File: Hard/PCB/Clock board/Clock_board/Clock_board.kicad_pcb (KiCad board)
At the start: 2 copper layers, 32.1 x 21 mm, 18 parts, among them J1 Conn_01x01, J2 Conn_01x01, J3 Conn_01x01, J4 Conn_01x01, J5 Conn_01x01, J6 Conn_01x01, M1 motor, Q1 SI2302, Q2 SI2302

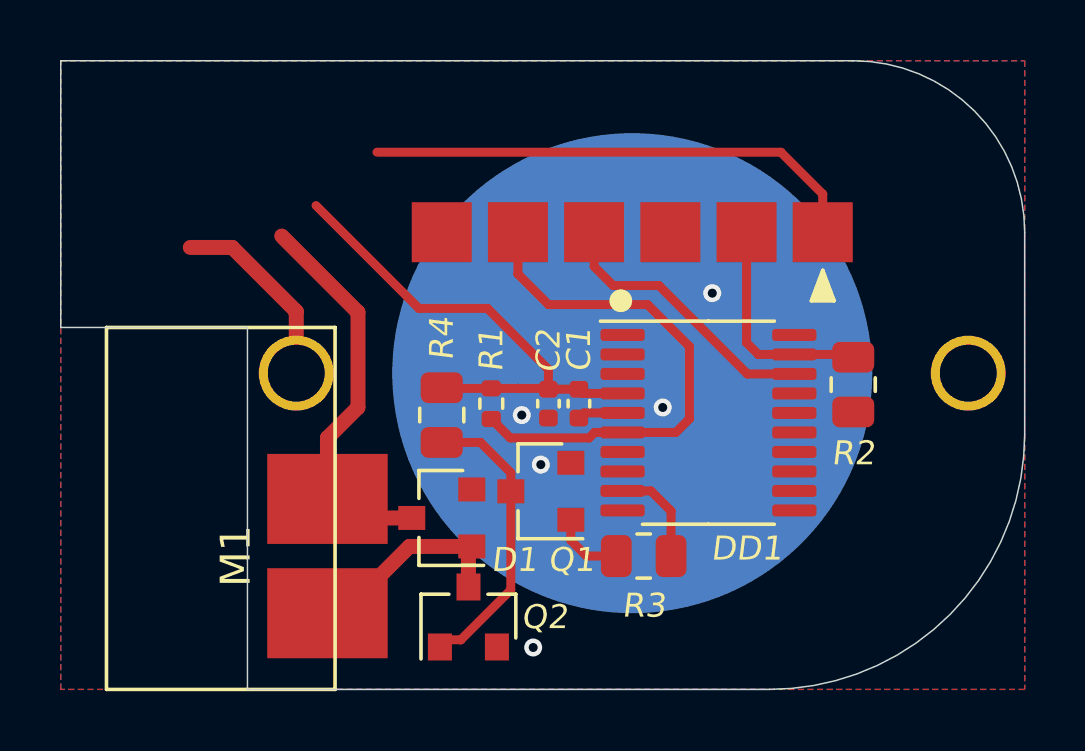
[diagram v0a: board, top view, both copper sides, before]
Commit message: shlyeha added switch component to mechanical library, changed scheme switch connection, finished pcb project
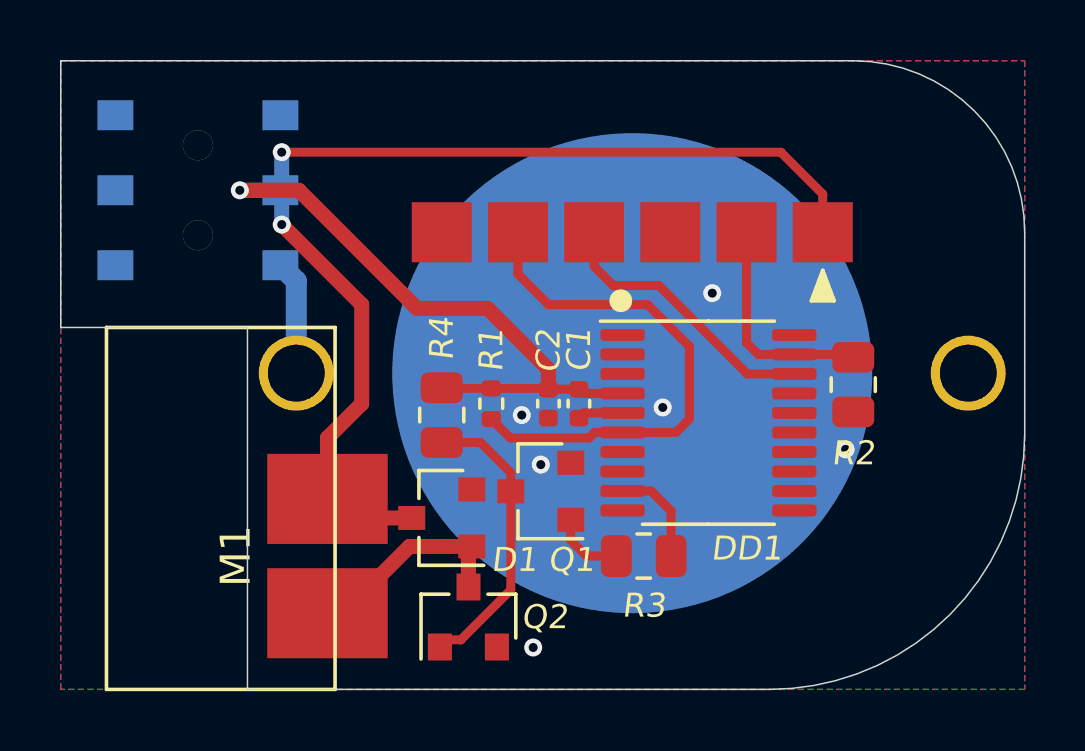
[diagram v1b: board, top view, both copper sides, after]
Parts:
- added SW1: SW_DPDT_x2, mechanical:switch_ms-22c01, B.Cu at (121.4, 74.8)
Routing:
- net +3V0: track 46.8 -> 57.0 mm, vias 0 -> 3
- net Net-(BT1-Pad1): track 6.47 -> 3.88 mm
- net GND: vias 5 -> 6
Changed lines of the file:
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@@
     (thickness 1.6)
     (drawings 13)
-    (tracks 69)
+    (tracks 80)
     (zones 0)
-    (modules 18)
-    (nets 27)
+    (modules 19)
+    (nets 28)
   )
   (page A4)
@@
   (net 25 /SWO)
   (net 26 "Net-(BT1-Pad1)")
+  (net 27 "Net-(SW1-Pad1)")
   (net_class Default "This is the default net class."
     (clearance 0.2)
@@
     (add_net "Net-(Q1-Pad1)")
     (add_net "Net-(Q1-Pad3)")
+    (add_net "Net-(SW1-Pad1)")
   )
   (module mechanical:motor_xiaomi_redmi_3s (layer F.Cu)
@@
       (scale (xyz 1 1 1))
       (rotate (xyz 0 180 0))
+    )
+  )
+  (module mechanical:switch_ms-22c01 (layer B.Cu)
+    (at 121.412 74.803 270)
+    (fp_text reference SW1 (at -3.429 -4.699) (layer B.SilkS)
+      (effects (font (size 0.8 0.8) (thickness 0.2) italic) (justify mirror))
+    )
+    (fp_text value SW_DPDT_x2 (at 0 0.5 270) (layer B.Fab) hide
+      (effects (font (size 1 1) (thickness 0.15)) (justify mirror))
+    )
+    (fp_line (start -3.81 -3.429) (end -3.81 3.429) (layer B.SilkS) (width 0.12))
+    (fp_line (start 3.81 -3.429) (end -3.81 -3.429) (layer B.SilkS) (width 0.12))
+    (fp_line (start 3.81 3.429) (end 3.81 -3.429) (layer B.SilkS) (width 0.12))
+    (fp_line (start -3.81 3.429) (end 3.81 3.429) (layer B.SilkS) (width 0.12))
+    (pad 6 smd rect (at -2.5 2.75 270) (size 1 1.2) (layers B.Cu B.Paste B.Mask))
+    (pad 5 smd rect (at 0 2.75 270) (size 1 1.2) (layers B.Cu B.Paste B.Mask))
+    (pad 4 smd rect (at 2.5 2.75 270) (size 1 1.2) (layers B.Cu B.Paste B.Mask))
+    (pad 3 smd rect (at 2.5 -2.75 270) (size 1 1.2) (layers B.Cu B.Paste B.Mask)
+      (net 26 "Net-(BT1-Pad1)"))
+    (pad 2 smd rect (at 0 -2.75 270) (size 1 1.2) (layers B.Cu B.Paste B.Mask)
+      (net 2 +3V0))
+    (pad 1 smd rect (at -2.5 -2.75 270) (size 1 1.2) (layers B.Cu B.Paste B.Mask)
+      (net 27 "Net-(SW1-Pad1)"))
+    (pad 0 thru_hole circle (at 1.5 0 270) (size 1 1) (drill 1) (layers *.Cu *.Mask))
+    (pad 0 thru_hole circle (at -1.5 0 270) (size 1 1) (drill 1) (layers *.Cu *.Mask))
+    (model C:/GitRepos/Archer/Hard/3D/STEP/g-switch_ms-22c01-g010.step
+      (at (xyz 0 0 0))
+      (scale (xyz 1 1 1))
+      (rotate (xyz 0 0 0))
     )
   )
@@
   (gr_line (start 141.859 78.486) (end 142.621 78.486) (layer F.SilkS) (width 0.12))
   (gr_line (start 142.24 77.47) (end 141.859 78.486) (layer F.SilkS) (width 0.12))
+  (via (at 143.002 83.439) (size 0.6) (drill 0.3) (layers F.Cu B.Cu) (net 1))
+  (via (at 122.809 74.803) (size 0.6) (drill 0.3) (layers F.Cu B.Cu) (net 2))
+  (via (at 124.206 73.533) (size 0.6) (drill 0.3) (layers F.Cu B.Cu) (net 2))
+  (via (at 124.206 75.946) (size 0.6) (drill 0.3) (layers F.Cu B.Cu) (net 2))
   (via (at 132.588 90.043) (size 0.6) (drill 0.3) (layers F.Cu B.Cu) (net 1))
   (via (at 138.557 78.232) (size 0.6) (drill 0.3) (layers F.Cu B.Cu) (net 1))
@@
   (segment (start 142.24 76.2) (end 142.24 74.93) (width 0.3) (layer F.Cu) (net 2))
   (segment (start 142.24 74.93) (end 140.843 73.533) (width 0.3) (layer F.Cu) (net 2))
-  (segment (start 140.843 73.533) (end 127.381 73.533) (width 0.3) (layer F.Cu) (net 2))
+  (segment (start 126.873 78.613) (end 124.206 75.946) (width 0.5) (layer F.Cu) (net 2))
+  (segment (start 126.873 81.915) (end 126.873 78.613) (width 0.5) (layer F.Cu) (net 2))
+  (segment (start 125.73 83.058) (end 126.873 81.915) (width 0.5) (layer F.Cu) (net 2))
   (segment (start 125.73 85.09) (end 125.73 83.058) (width 0.5) (layer F.Cu) (net 2))
-  (segment (start 125.73 83.058) (end 126.746 82.042) (width 0.5) (layer F.Cu) (net 2))
-  (segment (start 126.746 82.042) (end 126.746 78.867) (width 0.5) (layer F.Cu) (net 2))
-  (segment (start 126.746 78.867) (end 124.206 76.327) (width 0.5) (layer F.Cu) (net 2))
-  (segment (start 133.096 81.435) (end 133.096 80.772) (width 0.3) (layer F.Cu) (net 2))
-  (segment (start 133.096 80.772) (end 131.064 78.74) (width 0.3) (layer F.Cu) (net 2))
-  (segment (start 131.064 78.74) (end 128.778 78.74) (width 0.3) (layer F.Cu) (net 2))
-  (segment (start 128.778 78.74) (end 125.349 75.311) (width 0.3) (layer F.Cu) (net 2))
+  (segment (start 140.843 73.533) (end 124.206 73.533) (width 0.3) (layer F.Cu) (net 2))
+  (segment (start 124.206 74.759) (end 124.162 74.803) (width 0.3) (layer B.Cu) (net 2))
+  (segment (start 124.206 73.533) (end 124.206 74.759) (width 0.5) (layer B.Cu) (net 2))
+  (segment (start 124.206 74.847) (end 124.162 74.803) (width 0.3) (layer B.Cu) (net 2))
+  (segment (start 124.206 75.946) (end 124.206 74.847) (width 0.5) (layer B.Cu) (net 2))
+  (segment (start 124.162 74.803) (end 122.809 74.803) (width 0.5) (layer B.Cu) (net 2))
+  (segment (start 124.7775 74.803) (end 122.809 74.803) (width 0.5) (layer F.Cu) (net 2))
+  (segment (start 128.7145 78.74) (end 124.7775 74.803) (width 0.5) (layer F.Cu) (net 2))
+  (segment (start 131.064 78.74) (end 128.7145 78.74) (width 0.5) (layer F.Cu) (net 2))
+  (segment (start 133.096 80.772) (end 131.064 78.74) (width 0.5) (layer F.Cu) (net 2))
+  (segment (start 133.096 81.435) (end 133.096 80.772) (width 0.5) (layer F.Cu) (net 2))
   (segment (start 130.429 86.786) (end 130.54 86.675) (width 0.25) (layer F.Cu) (net 4))
   (segment (start 130.429 88.027) (end 130.429 86.786) (width 0.5) (layer F.Cu) (net 4))
@@
   (segment (start 137.1835 85.4945) (end 137.1835 86.995) (width 0.3) (layer F.Cu) (net 24))
   (segment (start 136.514 84.825) (end 137.1835 85.4945) (width 0.3) (layer F.Cu) (net 24))
-  (segment (start 122.555 76.708) (end 121.158 76.708) (width 0.5) (layer F.Cu) (net 26))
-  (segment (start 124.69 78.843) (end 122.555 76.708) (width 0.5) (layer F.Cu) (net 26))
-  (segment (start 124.69 80.899) (end 124.69 78.843) (width 0.5) (layer F.Cu) (net 26))
+  (segment (start 124.206 77.347) (end 124.162 77.303) (width 0.3) (layer B.Cu) (net 26))
+  (segment (start 124.162 77.303) (end 124.166 77.303) (width 0.3) (layer B.Cu) (net 26))
+  (segment (start 124.69 77.827) (end 124.69 80.899) (width 0.7) (layer B.Cu) (net 26))
+  (segment (start 124.166 77.303) (end 124.69 77.827) (width 0.7) (layer B.Cu) (net 26))
   (zone (net 1) (net_name GND) (layer F.Cu) (hatch edge 0.508)
     (connect_pads (clearance 0.1))
